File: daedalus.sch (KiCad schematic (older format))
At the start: 100 parts, among them J1 CAN Bus, J2 CAN Bus, J5 A Terminal, J6 B Terminal, J7 C Terminal, J9 USB_B_Micro, Q1 AO3401A, U1 XT30, U10 TPH, U11 TPH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

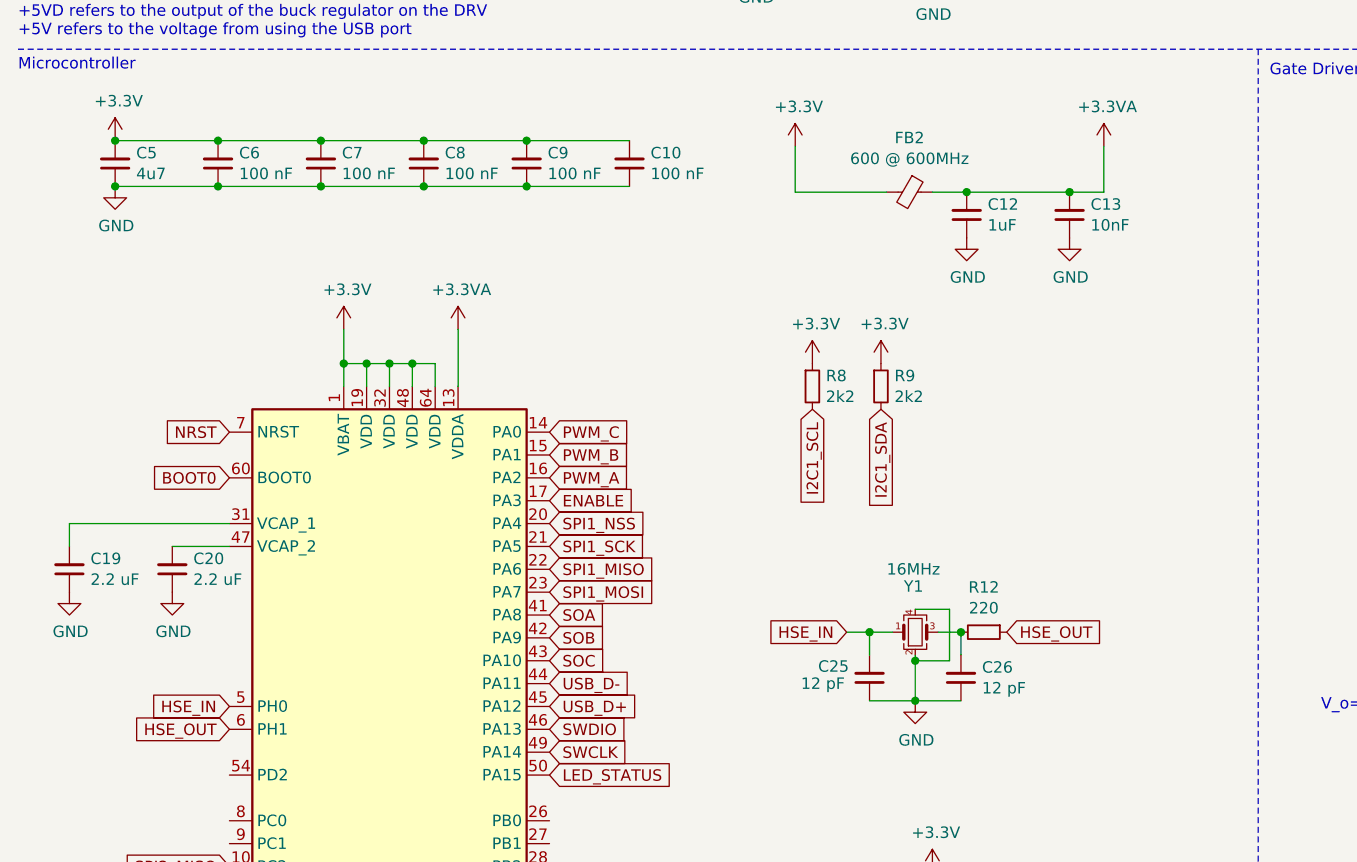
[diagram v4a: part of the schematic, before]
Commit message: Finished preliminary BOM
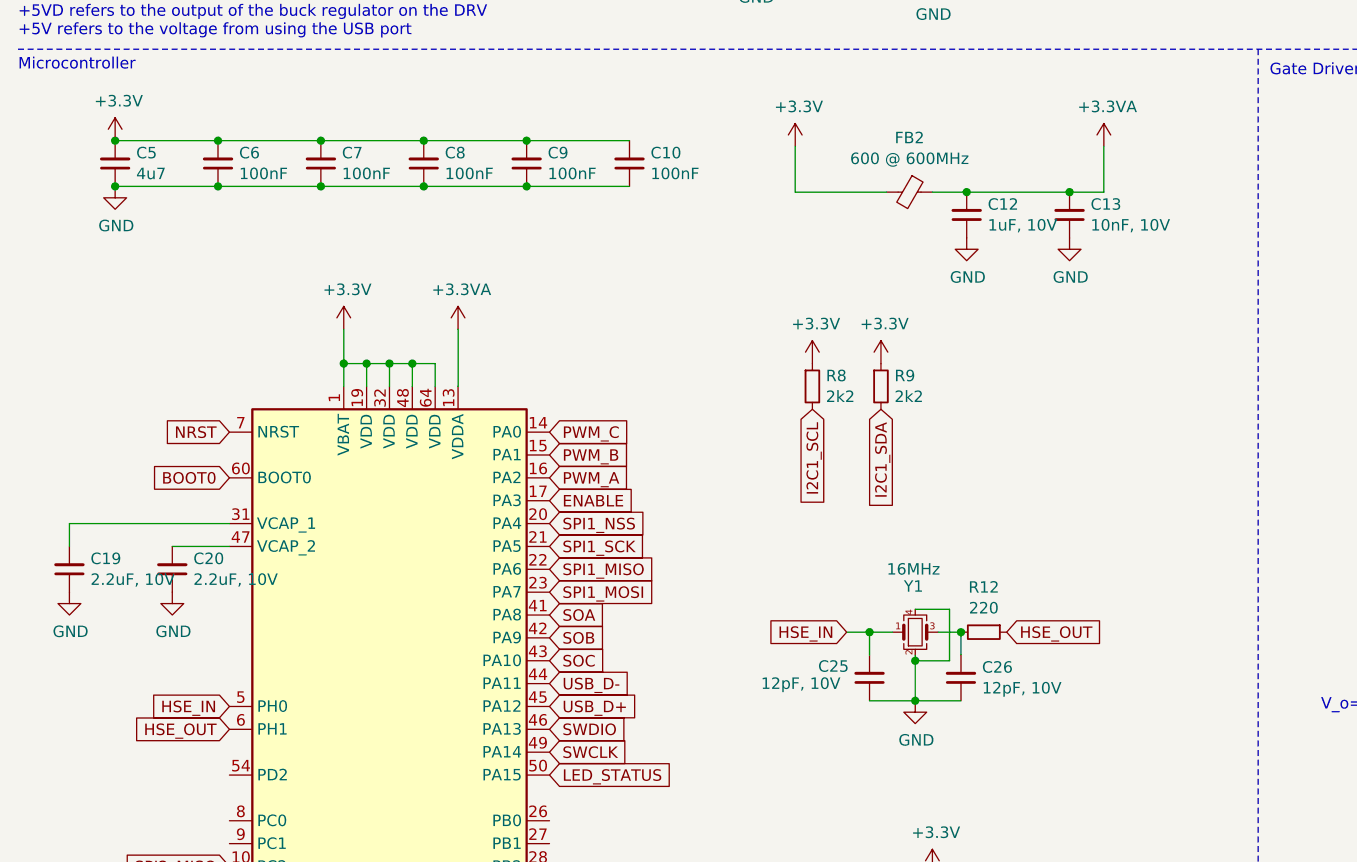
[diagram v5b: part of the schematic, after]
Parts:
- C10, C6, C7, C8, C9: value 100 nF -> 100nF
- C11, C23, C24: footprint Capacitor_SMD:C_0603_1608Metric -> Capacitor_SMD:C_0402_1005Metric
- C12: value 1uF -> 1uF, 10V
- C13: value 10nF -> 10nF, 10V
- C19, C20: value 2.2 uF -> 2.2uF, 10V
- C25, C26: value 12 pF -> 12pF, 10V
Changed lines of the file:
@@
 P 4625 2725
 F 0 "C12" H 4533 2679 50  0000 R CNN
-F 1 "1uF" H 4533 2770 50  0000 R CNN
+F 1 "1uF, 10V" H 4533 2770 50  0000 R CNN
 F 2 "Capacitor_SMD:C_0402_1005Metric" H 4625 2725 50  0001 C CNN
 F 3 "~" H 4625 2725 50  0001 C CNN
@@
 P 5075 2725
 F 0 "C13" H 4983 2679 50  0000 R CNN
-F 1 "10nF" H 4983 2770 50  0000 R CNN
+F 1 "10nF, 10V" H 4983 2770 50  0000 R CNN
 F 2 "Capacitor_SMD:C_0402_1005Metric" H 5075 2725 50  0001 C CNN
 F 3 "~" H 5075 2725 50  0001 C CNN
@@
 P 1150 4275
 F 0 "C20" H 1058 4229 50  0000 R CNN
-F 1 "2.2 uF" H 1058 4320 50  0000 R CNN
+F 1 "2.2uF, 10V" H 1058 4320 50  0000 R CNN
 F 2 "Capacitor_SMD:C_0603_1608Metric" H 1150 4275 50  0001 C CNN
 F 3 "~" H 1150 4275 50  0001 C CNN
@@
 P 700 4275
 F 0 "C19" H 608 4229 50  0000 R CNN
-F 1 "2.2 uF" H 608 4320 50  0000 R CNN
+F 1 "2.2uF, 10V" H 608 4320 50  0000 R CNN
 F 2 "Capacitor_SMD:C_0603_1608Metric" H 700 4275 50  0001 C CNN
 F 3 "~" H 700 4275 50  0001 C CNN
@@
 P 3150 2500
 F 0 "C10" H 3058 2454 50  0000 R CNN
-F 1 "100 nF" H 3058 2545 50  0000 R CNN
+F 1 "100nF" H 3058 2545 50  0000 R CNN
 F 2 "Capacitor_SMD:C_0402_1005Metric" H 3150 2500 50  0001 C CNN
 F 3 "~" H 3150 2500 50  0001 C CNN
@@
 P 2700 2500
 F 0 "C9" H 2608 2454 50  0000 R CNN
-F 1 "100 nF" H 2608 2545 50  0000 R CNN
+F 1 "100nF" H 2608 2545 50  0000 R CNN
 F 2 "Capacitor_SMD:C_0402_1005Metric" H 2700 2500 50  0001 C CNN
 F 3 "~" H 2700 2500 50  0001 C CNN
@@
 P 2250 2500
 F 0 "C8" H 2158 2454 50  0000 R CNN
-F 1 "100 nF" H 2158 2545 50  0000 R CNN
+F 1 "100nF" H 2158 2545 50  0000 R CNN
 F 2 "Capacitor_SMD:C_0402_1005Metric" H 2250 2500 50  0001 C CNN
 F 3 "~" H 2250 2500 50  0001 C CNN
@@
 P 1800 2500
 F 0 "C7" H 1708 2454 50  0000 R CNN
-F 1 "100 nF" H 1708 2545 50  0000 R CNN
+F 1 "100nF" H 1708 2545 50  0000 R CNN
 F 2 "Capacitor_SMD:C_0402_1005Metric" H 1800 2500 50  0001 C CNN
 F 3 "~" H 1800 2500 50  0001 C CNN
@@
 P 1350 2500
 F 0 "C6" H 1258 2454 50  0000 R CNN
-F 1 "100 nF" H 1258 2545 50  0000 R CNN
+F 1 "100nF" H 1258 2545 50  0000 R CNN
 F 2 "Capacitor_SMD:C_0402_1005Metric" H 1350 2500 50  0001 C CNN
 F 3 "~" H 1350 2500 50  0001 C CNN
@@
 P 4200 4750
 F 0 "C25" H 4425 4700 50  0000 R CNN
-F 1 "12 pF" H 4500 4775 50  0000 R CNN
+F 1 "12pF, 10V" H 4675 4775 50  0000 R CNN
 F 2 "Capacitor_SMD:C_0402_1005Metric" H 4200 4750 50  0001 C CNN
 F 3 "~" H 4200 4750 50  0001 C CNN
@@
 P 4600 4750
 F 0 "C26" H 4508 4704 50  0000 R CNN
-F 1 "12 pF" H 4508 4795 50  0000 R CNN
+F 1 "12pF, 10V" H 4508 4795 50  0000 R CNN
 F 2 "Capacitor_SMD:C_0402_1005Metric" H 4600 4750 50  0001 C CNN
 F 3 "~" H 4600 4750 50  0001 C CNN
@@
 F 0 "C23" H 12892 5521 50  0000 L CNN
 F 1 "0.1uF, 10V" H 12892 5430 50  0000 L CNN
-F 2 "Capacitor_SMD:C_0603_1608Metric" H 12800 5475 50  0001 C CNN
+F 2 "Capacitor_SMD:C_0402_1005Metric" H 12800 5475 50  0001 C CNN
 F 3 "~" H 12800 5475 50  0001 C CNN
 	1    12800 5475
@@
 F 0 "C24" H 13517 5521 50  0000 L CNN
 F 1 "0.1uF, 10V" H 13517 5430 50  0000 L CNN
-F 2 "Capacitor_SMD:C_0603_1608Metric" H 13425 5475 50  0001 C CNN
+F 2 "Capacitor_SMD:C_0402_1005Metric" H 13425 5475 50  0001 C CNN
 F 3 "~" H 13425 5475 50  0001 C CNN
 	1    13425 5475
@@
 F 0 "C11" H 13767 3196 50  0000 L CNN
 F 1 "0.1uF, 10V" H 13767 3105 50  0000 L CNN
-F 2 "Capacitor_SMD:C_0603_1608Metric" H 13675 3150 50  0001 C CNN
+F 2 "Capacitor_SMD:C_0402_1005Metric" H 13675 3150 50  0001 C CNN
 F 3 "~" H 13675 3150 50  0001 C CNN
 	1    13675 3150

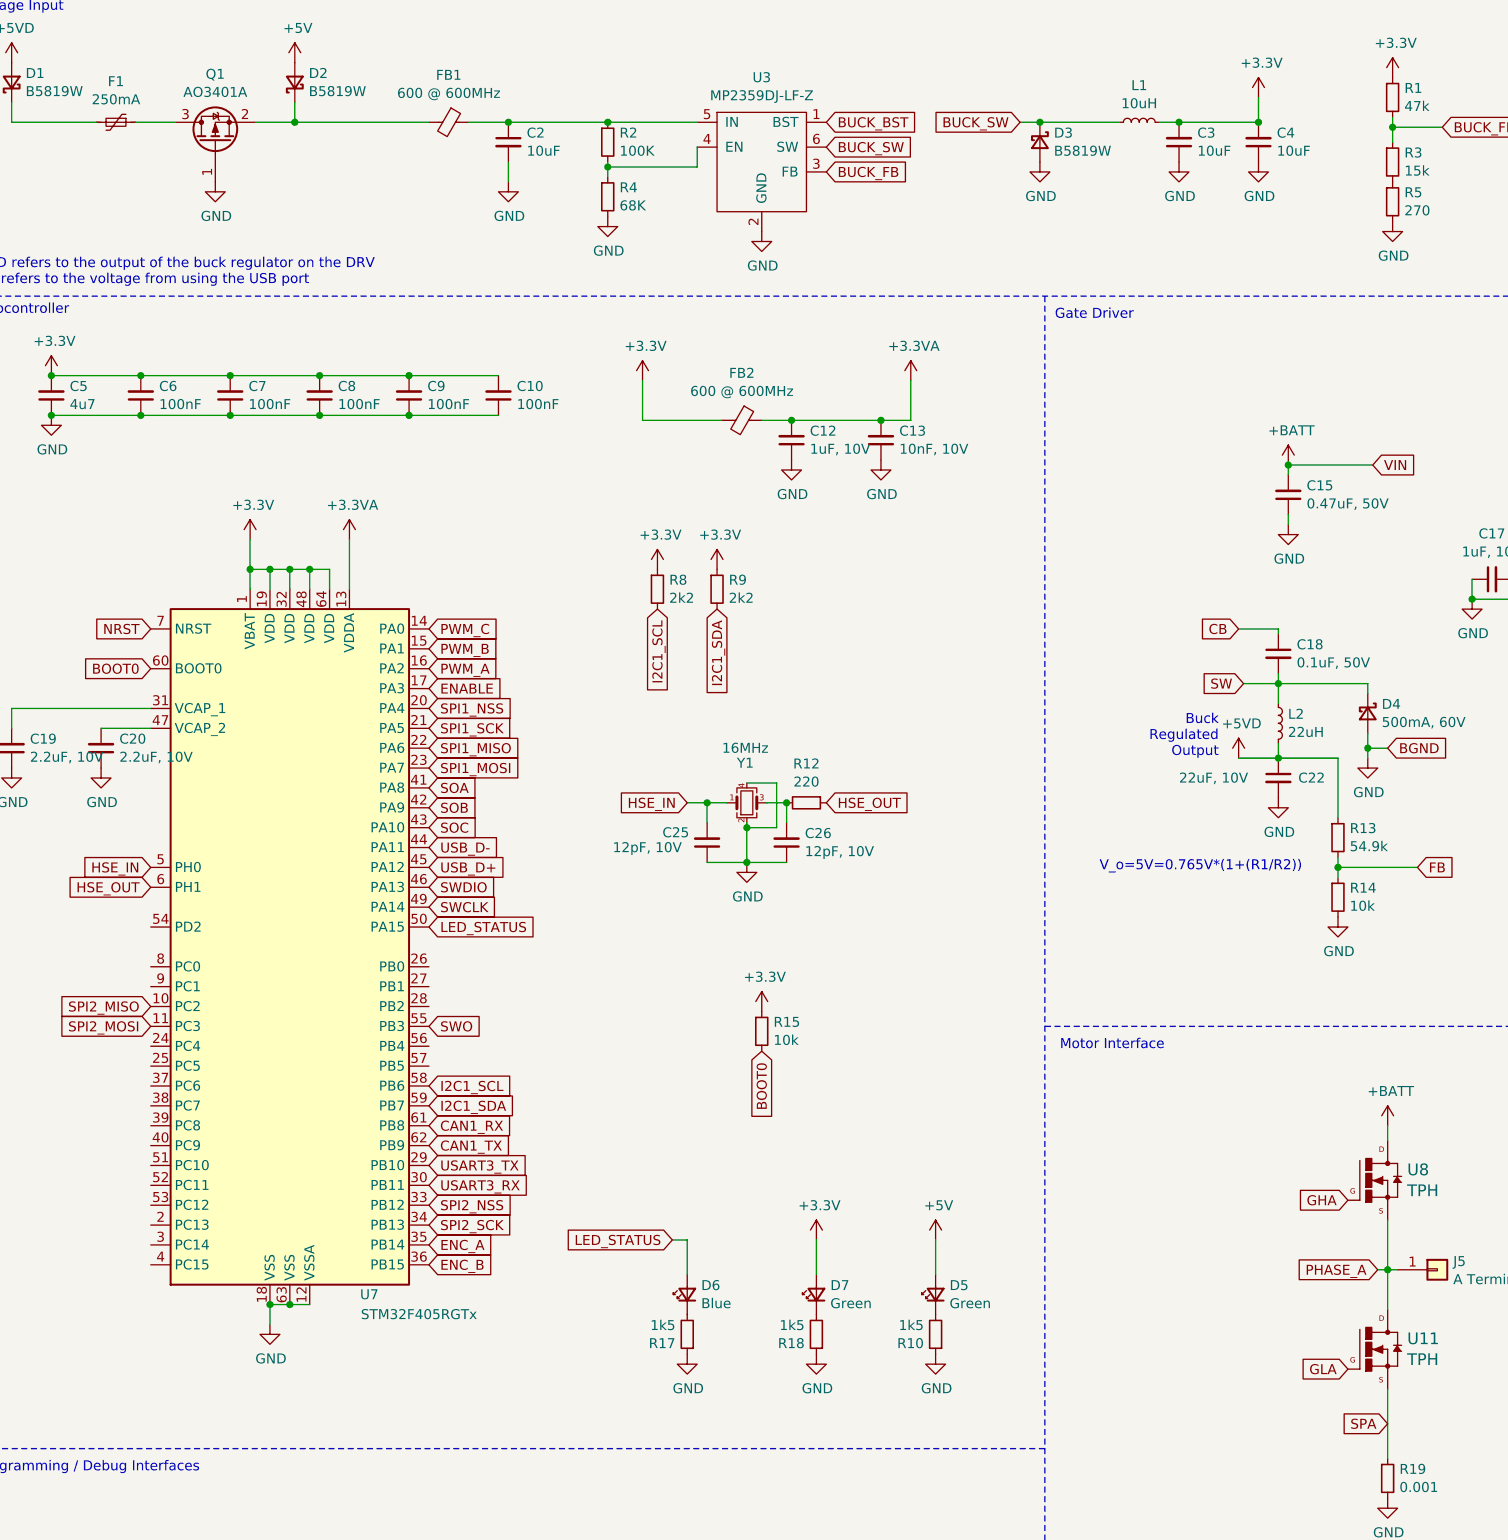
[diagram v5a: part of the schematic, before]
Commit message: Updated vias, added vias, removed i2c line and pullups, added renders
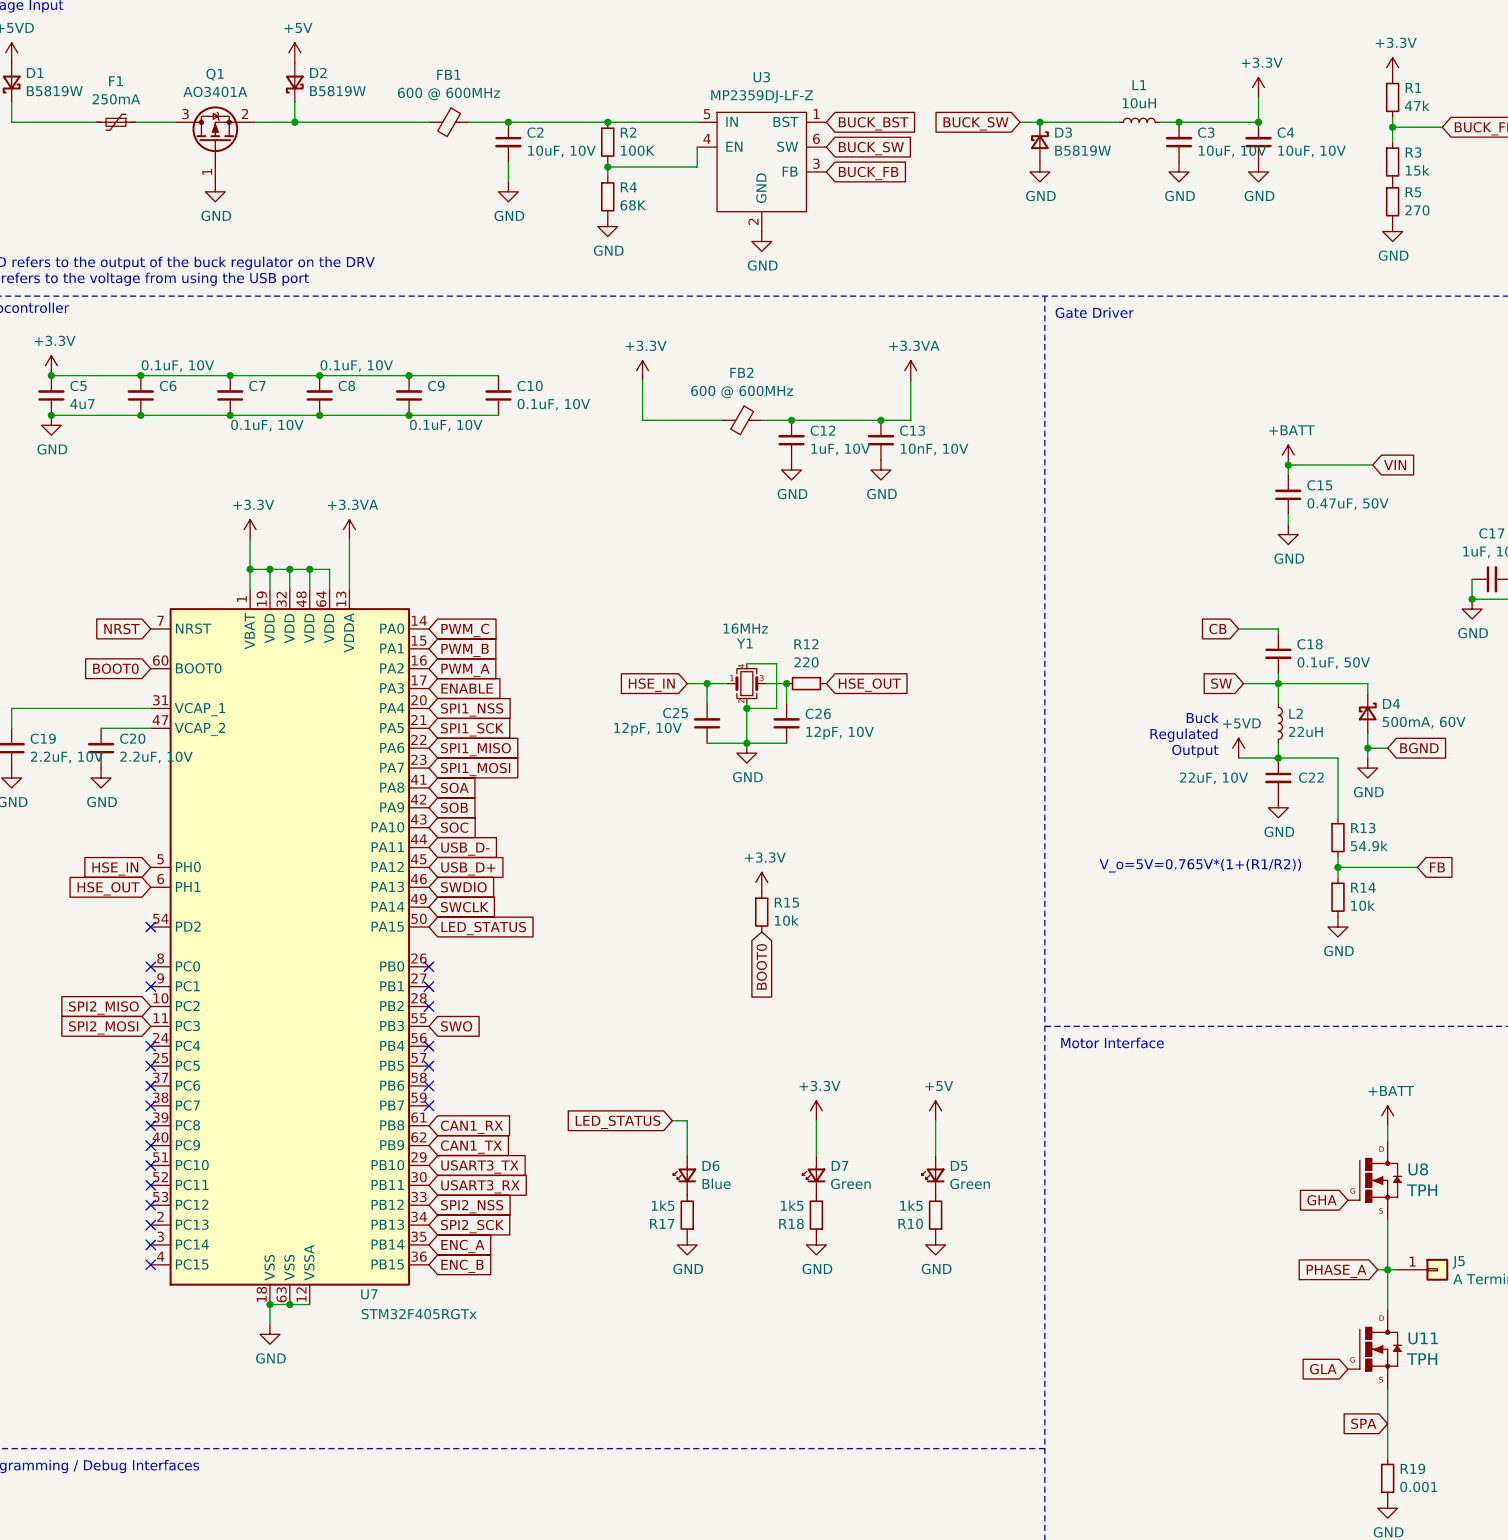
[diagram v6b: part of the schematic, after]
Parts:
- removed R8, R9: 2k2, Resistor_SMD:R_0402_1005Metric, symbol Device:R_Small
- C10, C6, C7, C8, C9: value 100nF -> 0.1uF, 10V
- C2, C3, C4: value 10uF -> 10uF, 10V
- J5, J6, J7: footprint TestPoint:TestPoint_Pad_3.0x3.0mm -> daedalus_kicad_lib:18_AWG_PAD
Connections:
- net I2C1_SCL: no longer names the net of U7.58 (PB6)
- net I2C1_SDA: no longer names the net of U7.59 (PB7)
- no-connect marks 7 -> 29
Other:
- moved on the sheet: C25, C26, D5, D6, D7, R10, R12, R15, R17, R18, Y1
